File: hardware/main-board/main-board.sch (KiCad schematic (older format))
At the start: 92 parts, among them J1 BARREL_JACK, J2 CONN_01X10, J3 CONN_01X10, J4 USB_OTG, J5 CONN_02X05, J6 SMA, Q1 DDTD113ZC, Q2 DDTD113ZC, Q3 DDTD113ZC, Q4 DDTD113ZC, Q5 DDTD113ZC, Q6 FDB14N30TM, Q7 DDTD113ZC, Q8 DDTD113ZC, Q9 DDTD113ZC, SW1 SW_Push, SW2 SW_Push, SW3 SW_Push, SW4 SW_Push, SW5 SW_DIP_x01, U1 LD1117S33TR, U2 MAX1771, U3 STM32F302C, U4 FGPMMOPA6H, Y1 8MHz, Y2 32.768kHz

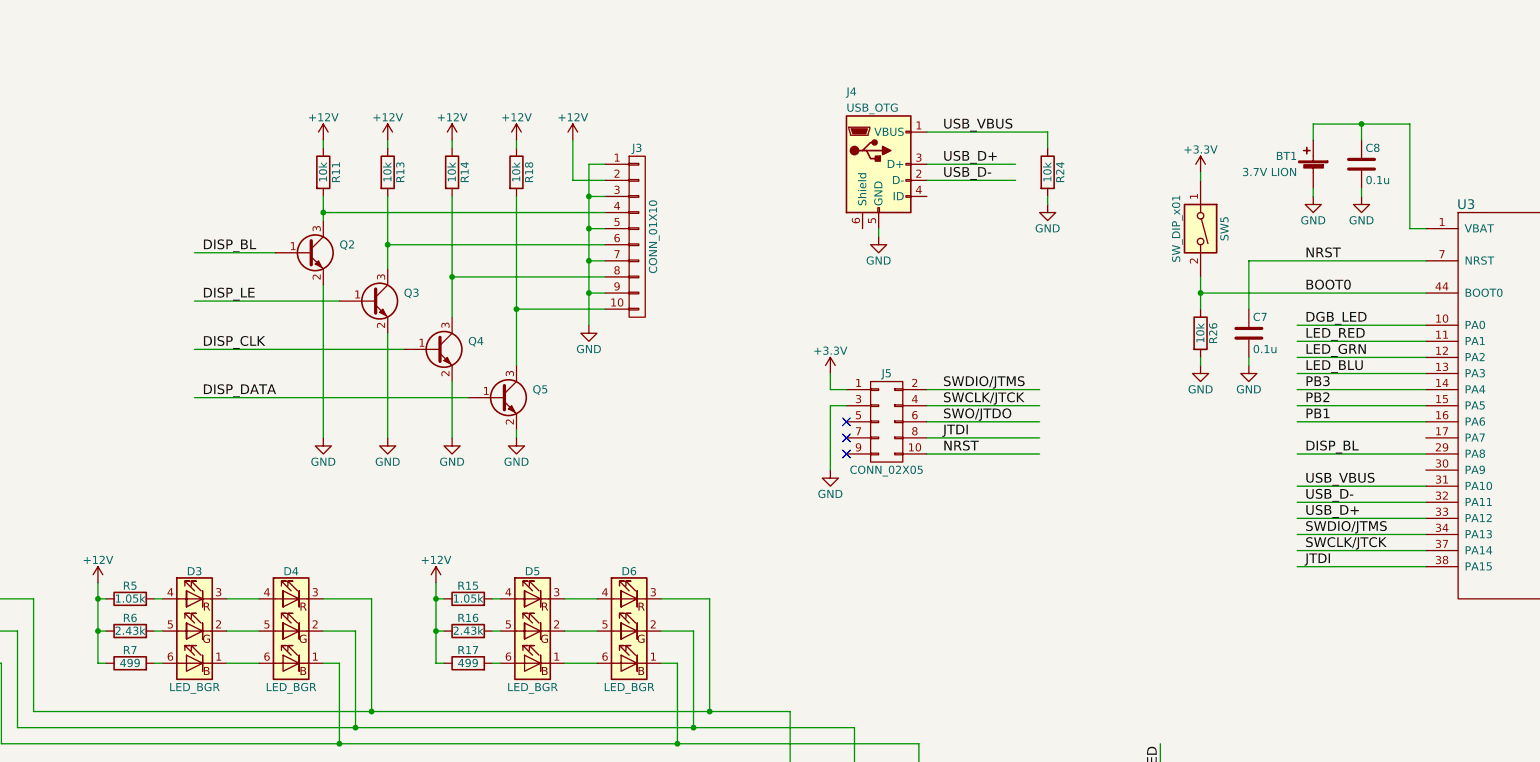
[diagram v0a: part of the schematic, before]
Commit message: Added pull up circuit for USB.  Changed boot switch to a right angle pushbutton so that it can be used to switch to bootloader mode within the enclosure
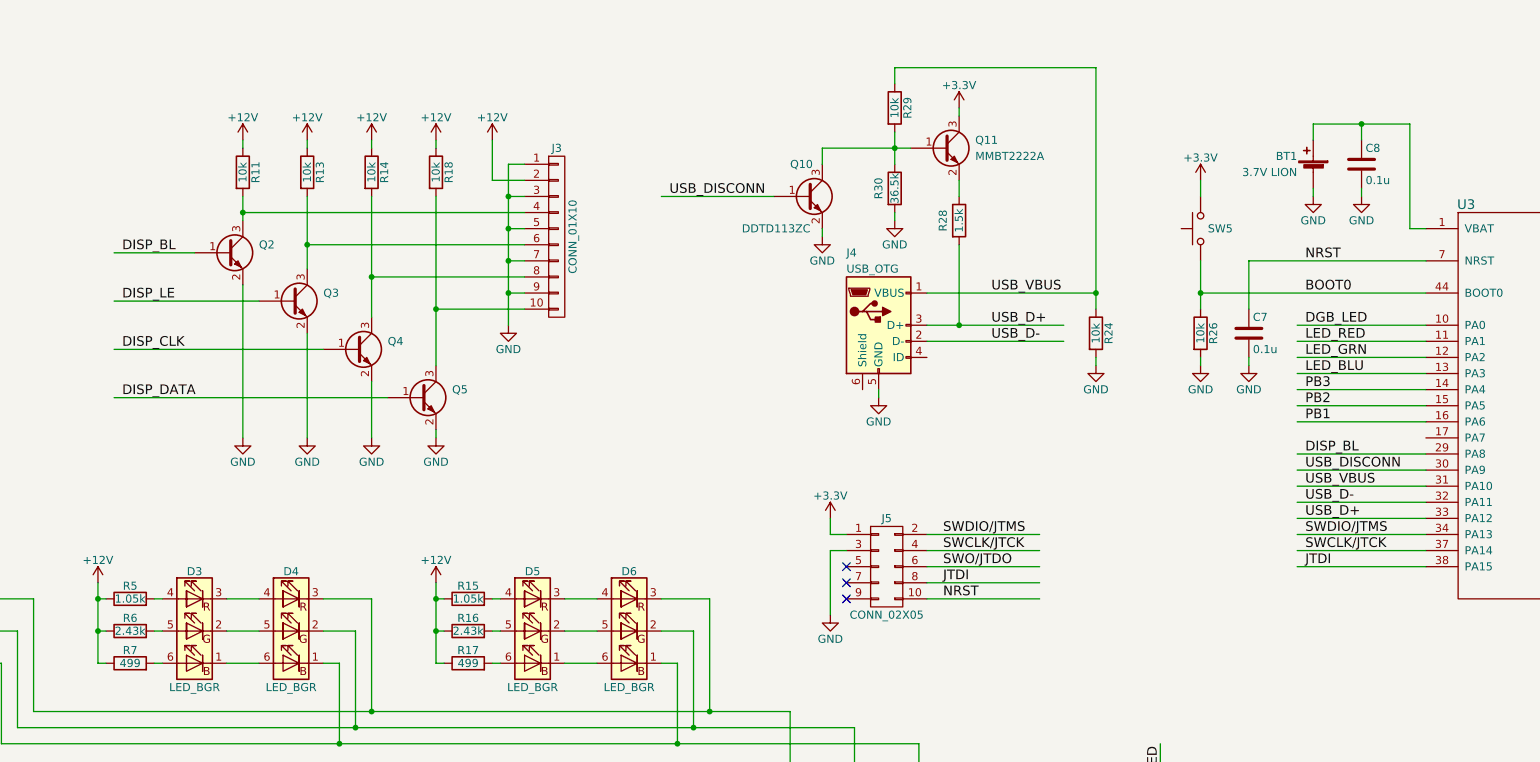
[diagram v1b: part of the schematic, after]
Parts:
- removed SW5: SW_DIP_x01, radio-clock:SDA01H1SBD, symbol SW_DIP_x01
- added Q10: DDTD113ZC, TO_SOT_Packages_SMD:SOT-23, symbol Q_NPN_BEC
- added Q11: MMBT2222A, TO_SOT_Packages_SMD:SOT-23, symbol Q_NPN_BEC
- added R28: 1.5k, Resistors_SMD:R_0805, symbol R
- added R29: 10k, Resistors_SMD:R_0805, symbol R
- added R30: 36.5k, Resistors_SMD:R_0805, symbol R
- added SW5: SW_Push, radio-clock:TL1105SF160Q, symbol SW_Push
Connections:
- net labels added: USB_DISCONN
- wire segments 291 -> 303
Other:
- moved on the sheet: J3, J4, J5, Q2, Q3, Q4, Q5, R11, R13, R14, R18, R24
